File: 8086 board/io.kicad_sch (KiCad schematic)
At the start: 69 parts, among them J2 RM68090, J3 RGB LCD, U22 74AC573, U23 74AC573, U26 74AC573, U27 74AC573, U28 74AC573, U29 74AC573, U3 74HC14, U30 74LVC245A, U31 74LVC245A, U32 74LVC245A, U4 74HC02

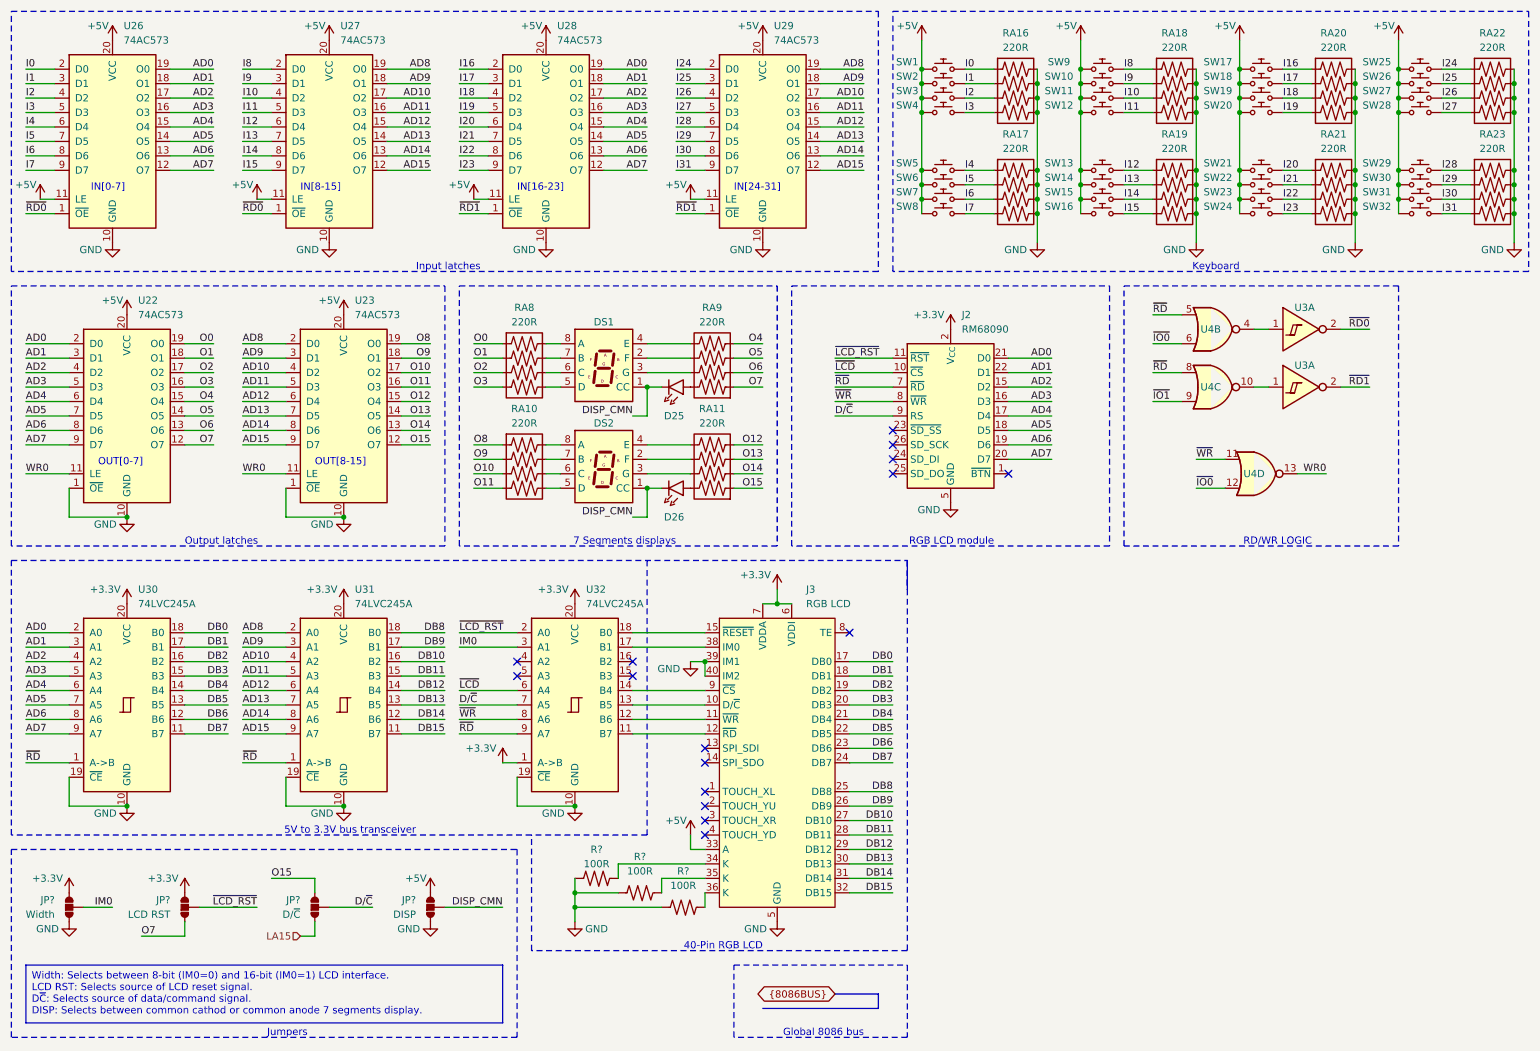
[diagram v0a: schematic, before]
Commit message: reduced schematic, PCB memory routed
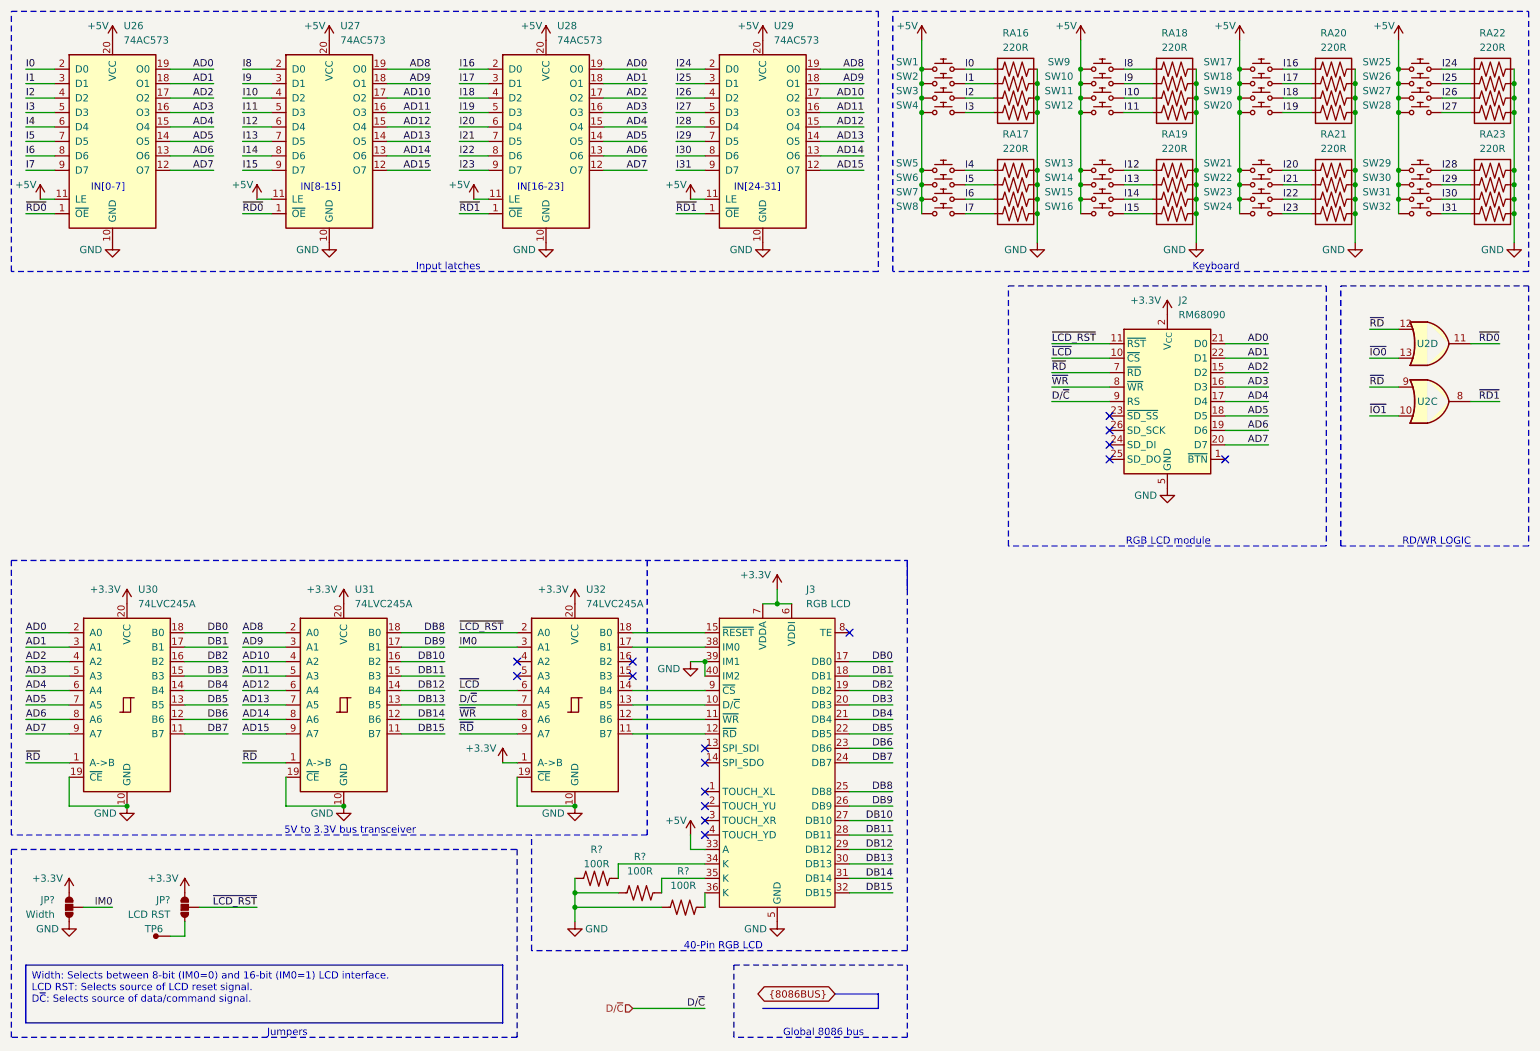
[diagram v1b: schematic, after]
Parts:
- removed D25, D26: LED, LED_SMD:LED_0603_1608Metric_Pad1.05x0.95mm_HandSolder, symbol 8086PC:LED
- removed DS1, DS2: 7SEG, 8086PC:2181AS, symbol 8086PC:2181AS
- removed JP?: DISP, Jumper:SolderJumper-3_P2.0mm_Open_TrianglePad1.0x1.5mm, symbol 8086PC:SolderJumper
- removed JP?: D/~{C}, Jumper:SolderJumper-3_P2.0mm_Open_TrianglePad1.0x1.5mm, symbol 8086PC:SolderJumper
- removed RA10, RA11, RA8, RA9: 220R, Resistor_SMD:R_Array_Concave_4x0603, symbol 8086PC:R_Array_4
- removed U22, U23: 74AC573, Package_SO:TSSOP-20_4.4x6.5mm_P0.65mm, symbol 8086PC:74AC573
- removed U3 (x2): 74HC14, Package_SO:SOIC-14_3.9x8.7mm_P1.27mm, symbol 8086PC:74HC14
- removed U4: 74HC02, Package_SO:SOIC-14_3.9x8.7mm_P1.27mm, symbol 8086PC:74HC02
- added TP6: ~, TestPoint:TestPoint_Pad_1.5x1.5mm, symbol 8086PC:TestPoint
- added U2: 74HC32, Package_SO:TSSOP-14_4.4x5mm_P0.65mm, symbol 8086PC:74HC32
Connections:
- net +3.3V: now also JP?.3, JP?.3; no longer JP?.2, JP?.2
- net IM0: now also JP?.2; no longer JP?.3
- net ~{IO0}: now also U2.13
- net ~{IO1}: now also U2.10
- net ~{LCD_RST}: now also JP?.2; no longer JP?.3
- net ~{RD0}: now also U2.11
- net ~{RD1}: now also U2.8
- net ~{RD}: now also U2.12, U2.9
- net O7: no longer names the net of JP?.1
- net O7: now also TP6.1
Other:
- note removed: "7 Segments displays"
- note removed: "OUT[0-7]"
- note removed: "OUT[8-15]"
- note removed: "Output latches"
- moved on the sheet: J2

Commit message: schematic: reduced 8086 bus, no LCD shield
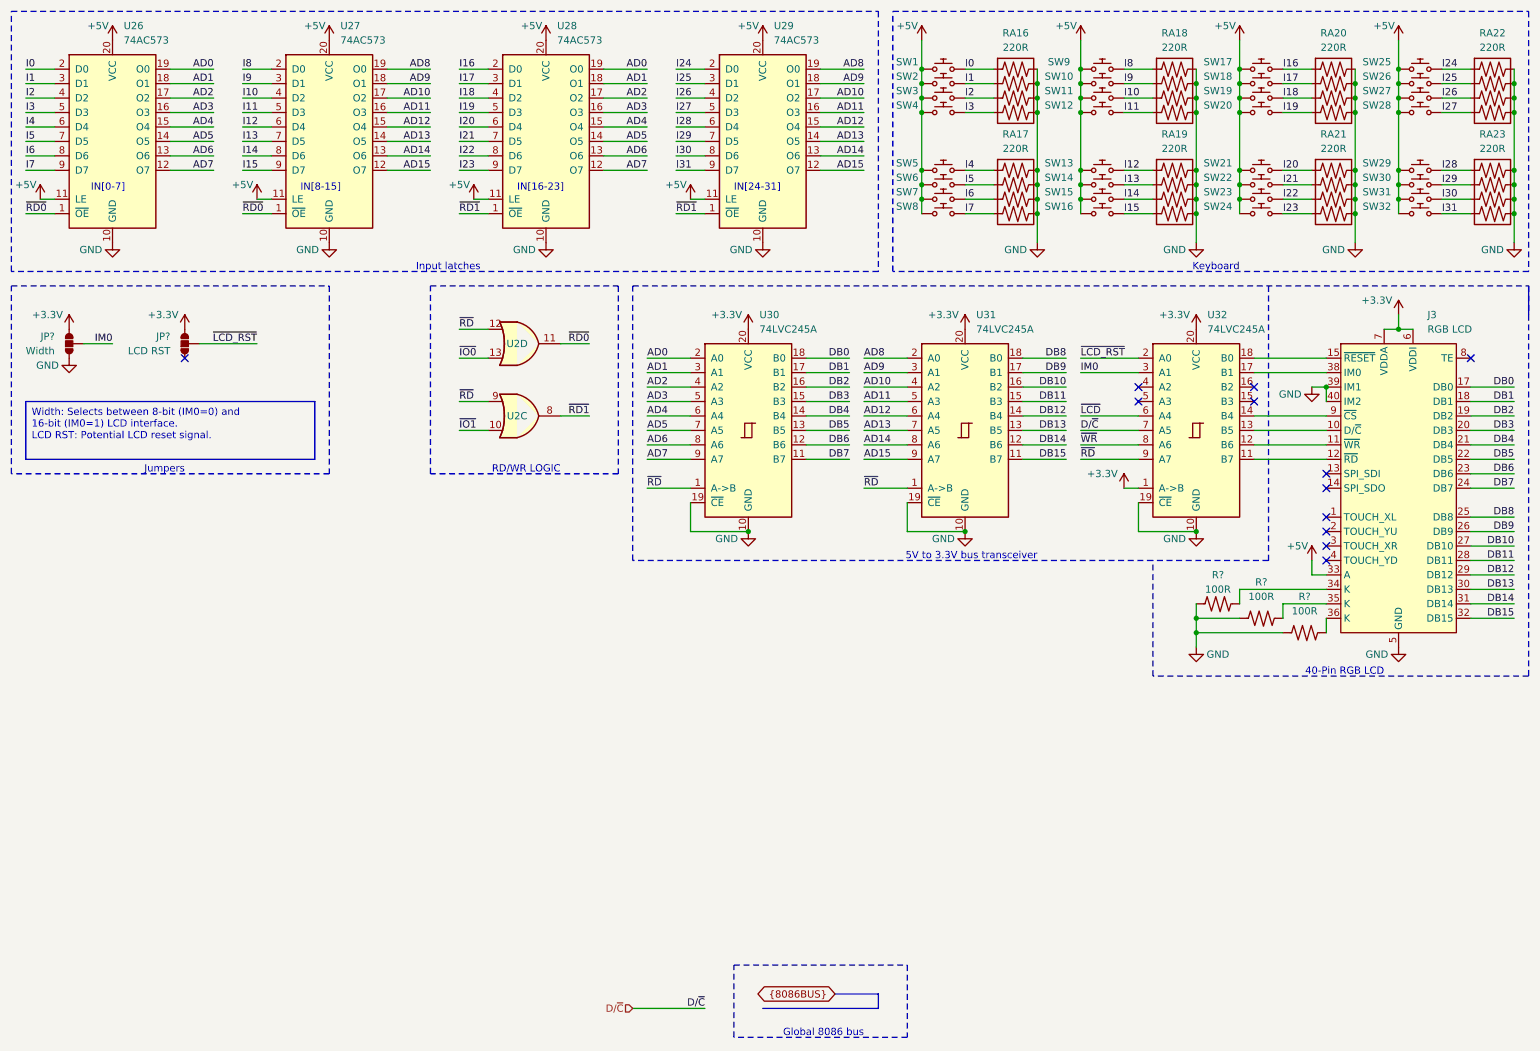
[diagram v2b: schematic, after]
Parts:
- removed J2: RM68090, 8086PC:RM68090 RGB LCD module, symbol 8086PC:RM68090
- removed TP6: ~, TestPoint:TestPoint_Pad_1.5x1.5mm, symbol 8086PC:TestPoint
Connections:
- no-connect marks 16 -> 12
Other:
- note removed: "RGB LCD module"
- moved on the sheet: J3, JP?, R?, U2C, U2D, U30, U31, U32

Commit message: PCB: more layout work. some schematic changes.
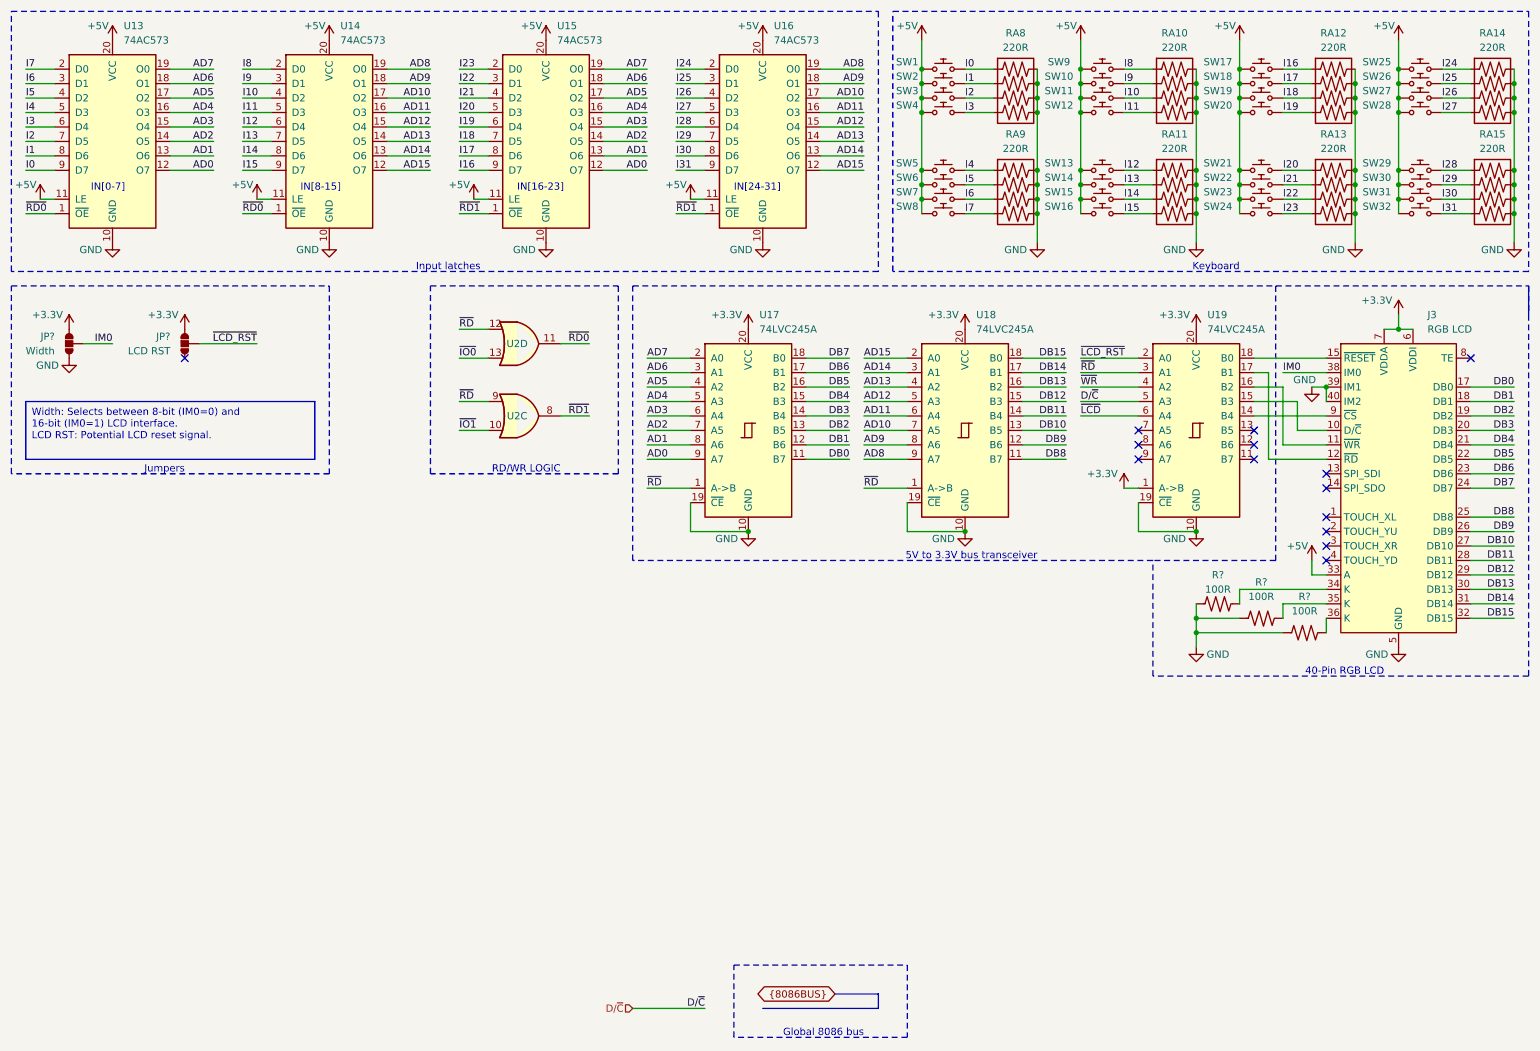
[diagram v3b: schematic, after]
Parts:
- JP? (x2): footprint Jumper:SolderJumper-3_P2.0mm_Open_TrianglePad1.0x1.5mm -> Jumper:SolderJumper-3_P1.3mm_Bridged12_RoundedPad1.0x1.5mm
- SW1, SW10, SW11, SW12, SW13, SW14, SW15, SW16, SW17, SW18, SW19, SW2, SW20, SW21, SW22, SW23, SW24, SW25, SW26, SW27, SW28, SW29, SW3, SW30, SW31, SW32, SW4, SW5, SW6, SW7, SW8, SW9: footprint 8086PC:SW_Push_1P1T_NO_6x6mm_H9.5mm -> 8086PC:SW_Push_6x6x5mm
- renumbered RA18 to RA10, RA19 to RA11, RA20 to RA12, RA21 to RA13, RA22 to RA14, RA23 to RA15, RA16 to RA8, RA17 to RA9, U26 to U13, U27 to U14, U28 to U15, U29 to U16, U30 to U17, U31 to U18, U32 to U19
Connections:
- net +3.3V: now also JP?.1, JP?.1; no longer JP?.3, JP?.3
- net AD0: now also U13.12 (O7), U15.12 (O7), U17.9 (A7); no longer U13.19 (O0), U15.19 (O0), U17.2 (A0)
- net AD1: now also U13.13 (O6), U15.13 (O6), U17.8 (A6); no longer U13.18 (O1), U15.18 (O1), U17.3 (A1)
- net AD10: now also U18.7 (A5); no longer U18.4 (A2)
- net AD11: now also U18.6 (A4); no longer U18.5 (A3)
- net AD12: now also U18.5 (A3); no longer U18.6 (A4)
- net AD13: now also U18.4 (A2); no longer U18.7 (A5)
- net AD14: now also U18.3 (A1); no longer U18.8 (A6)
- net AD15: now also U18.2 (A0); no longer U18.9 (A7)
- net AD2: now also U13.14 (O5), U15.14 (O5), U17.7 (A5); no longer U13.17 (O2), U15.17 (O2), U17.4 (A2)
- net AD3: now also U13.15 (O4), U15.15 (O4), U17.6 (A4); no longer U13.16 (O3), U15.16 (O3), U17.5 (A3)
- net AD4: now also U13.16 (O3), U15.16 (O3), U17.5 (A3); no longer U13.15 (O4), U15.15 (O4), U17.6 (A4)
- net AD5: now also U13.17 (O2), U15.17 (O2), U17.4 (A2); no longer U13.14 (O5), U15.14 (O5), U17.7 (A5)
- net AD6: now also U13.18 (O1), U15.18 (O1), U17.3 (A1); no longer U13.13 (O6), U15.13 (O6), U17.8 (A6)
- net AD7: now also U13.19 (O0), U15.19 (O0), U17.2 (A0); no longer U13.12 (O7), U15.12 (O7), U17.9 (A7)
- net AD8: now also U18.9 (A7); no longer U18.2 (A0)
- net AD9: now also U18.8 (A6); no longer U18.3 (A1)
- net DB0: now also U17.11 (B7); no longer U17.18 (B0)
- net DB1: now also U17.12 (B6); no longer U17.17 (B1)
- net DB10: now also U18.13 (B5); no longer U18.16 (B2)
- net DB11: now also U18.14 (B4); no longer U18.15 (B3)
- net DB12: now also U18.15 (B3); no longer U18.14 (B4)
- net DB13: now also U18.16 (B2); no longer U18.13 (B5)
- net DB14: now also U18.17 (B1); no longer U18.12 (B6)
- net DB15: now also U18.18 (B0); no longer U18.11 (B7)
- net DB2: now also U17.13 (B5); no longer U17.16 (B2)
- net DB3: now also U17.14 (B4); no longer U17.15 (B3)
- net DB4: now also U17.15 (B3); no longer U17.14 (B4)
- net DB5: now also U17.16 (B2); no longer U17.13 (B5)
- net DB6: now also U17.17 (B1); no longer U17.12 (B6)
- net DB7: now also U17.18 (B0); no longer U17.11 (B7)
- net DB8: now also U18.11 (B7); no longer U18.18 (B0)
- net DB9: now also U18.12 (B6); no longer U18.17 (B1)
- net D/~{C}: now also U19.5 (A3); no longer U19.7 (A5)
- net GND: now also JP?.3; no longer JP?.1
- net I0: now also U13.9 (D7); no longer U13.2 (D0)
- net I1: now also U13.8 (D6); no longer U13.3 (D1)
- net I16: now also U15.9 (D7); no longer U15.2 (D0)
- net I17: now also U15.8 (D6); no longer U15.3 (D1)
- net I18: now also U15.7 (D5); no longer U15.4 (D2)
- net I19: now also U15.6 (D4); no longer U15.5 (D3)
- net I2: now also U13.7 (D5); no longer U13.4 (D2)
- net I20: now also U15.5 (D3); no longer U15.6 (D4)
- net I21: now also U15.4 (D2); no longer U15.7 (D5)
- net I22: now also U15.3 (D1); no longer U15.8 (D6)
- net I23: now also U15.2 (D0); no longer U15.9 (D7)
- net I3: now also U13.6 (D4); no longer U13.5 (D3)
- net I4: now also U13.5 (D3); no longer U13.6 (D4)
- net I5: now also U13.4 (D2); no longer U13.7 (D5)
- net I6: now also U13.3 (D1); no longer U13.8 (D6)
- net I7: now also U13.2 (D0); no longer U13.9 (D7)
- net IM0: now also J3.38 (IM0); no longer U19.3 (A1)
- net ~{RD}: now also U19.3 (A1); no longer U19.9 (A7)
- net ~{WR}: now also U19.4 (A2); no longer U19.8 (A6)
- net at U19.11 (B7): no longer J3.12 (~{RD})
- net at U19.12 (B6): no longer J3.11 (~{WR})
- net at U19.13 (B5): no longer J3.10 (D/~{C})
- net at U19.15 (B3): now also J3.10 (D/~{C})
- net at U19.16 (B2): now also J3.11 (~{WR})
- net at U19.17 (B1): now also J3.12 (~{RD}); no longer J3.38 (IM0)
- no-connect marks 12 -> 14
